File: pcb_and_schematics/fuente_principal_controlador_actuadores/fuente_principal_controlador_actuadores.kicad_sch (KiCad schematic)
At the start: 79 parts, among them J1 Screw_Terminal_01x02, J1 USB3_A 1, J10 Screw_Terminal_01x02, J2 Screw_Terminal_01x02, J2 USB3_A 2, J3 Screw_Terminal_01x02, J3 USB3_A 3, J4 Screw_Terminal_01x02, J4 USB3_A 4, J5 Screw_Terminal_01x02, J6 Screw_Terminal_01x02, J7 Screw_Terminal_01x02, J8 Screw_Terminal_01x02, J9 Screw_Terminal_01x02, Q1 TIP122, Q2 TIP122, Q3 TIP122, Q4 TIP122, Q5 TIP122, Q6 TIP122, Q7 TIP122, Q8 TIP122, U1 40106, U1 LM7812_TO220, U11 40106, U2 LM7805_TO220, U22 40106, U3 LM1117-3.3, U33 40106, U44 40106, U55 40106, U66 40106

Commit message: new footprints added to the schematics, and save process before reestructuration of trigger schmith footprint and schematic
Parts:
- removed J1: USB3_A 1, symbol Connector:USB3_A
- removed J2: USB3_A 2, symbol Connector:USB3_A
- removed J3: USB3_A 3, symbol Connector:USB3_A
- removed J4: USB3_A 4, symbol Connector:USB3_A
- added J1, J2, J3, J4: USB_A, Connector_USB:USB_A_Molex_67643_Horizontal, symbol Connector:USB_A
- J11, J12: renamed from J?; footprint (none) -> Connector_PinSocket_1.27mm:PinSocket_1x15_P1.27mm_Vertical
- R_actuator1, R_actuator2, R_actuator3, R_actuator4, R_actuator5, R_actuator6, R_actuator7, R_actuator9, Rsensor1, Rsensor2: footprint (none) -> Resistor_THT:R_Axial_DIN0204_L3.6mm_D1.6mm_P5.08mm_Horizontal
- Rpullup1, Rpullup2, Rpullup3, Rpullup4, Rpullup5, Rpullup6, Rpullup7, Rpullup8, Rtransistor1, Rtransistor2, Rtransistor3, Rtransistor4, Rtransistor5, Rtransistor6, Rtransistor7, Rtransistor8: footprint (none) -> Resistor_THT:R_Axial_DIN0207_L6.3mm_D2.5mm_P7.62mm_Horizontal
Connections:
- net 3.3VDC: now also J2.1 (VBUS), J3.1 (VBUS), J4.1 (VBUS)
- net GND 3.3V: now also J2.4 (GND), J3.4 (GND), J4.4 (GND)
- net GND ec: now also J1.4 (GND)
- net Signal ExtraSensor: now also J4.3 (D+)
- net signal DB18B20: now also J2.3 (D+)
- net signal EC: now also J1.1 (VBUS), J1.3 (D+)
- net signal PH: now also J3.3 (D+)
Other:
- moved on the sheet: J10, J3, J4, J5, J6, J7, J8, J9, Opto1, Opto2, Opto3, Opto4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

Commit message: everything looks kinda ready for pcb fixies
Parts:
- removed J3, J4: Screw_Terminal_01x02, symbol Connector:Screw_Terminal_01x02
- removed Opto1, Opto2: 4N25, Package_DIP:DIP-6_W7.62mm, symbol Isolator:4N25
- removed Q1, Q2: TIP122, Package_TO_SOT_THT:TO-220-3_Vertical, symbol Transistor_BJT:TIP122
- removed R_actuator1, R_actuator2: 220 ohm, Resistor_THT:R_Axial_DIN0204_L3.6mm_D1.6mm_P5.08mm_Horizontal, symbol Device:R
- removed Rpullup1, Rpullup2: 10k ohm, Resistor_THT:R_Axial_DIN0207_L6.3mm_D2.5mm_P7.62mm_Horizontal, symbol Device:R
- removed Rtransistor1, Rtransistor2: 10 ohm, Resistor_THT:R_Axial_DIN0207_L6.3mm_D2.5mm_P7.62mm_Horizontal, symbol Device:R
- removed U1, U11, U22, U33, U44, U55, U66: 40106, symbol 4xxx:40106
- removed unit 2 of U2
- added J5, J8: Screw_Terminal_01x02, maticas:actuators_screws_01x02_low_pot, symbol Connector:Screw_Terminal_01x02
- added Opto3, Opto6: 4N25, Package_DIP:DIP-6_W7.62mm, symbol Isolator:4N25
- added Q3, Q6: TIP122, Package_TO_SOT_THT:TO-220-3_Vertical, symbol Transistor_BJT:TIP122
- added R_actuator3, R_actuator6: 220 ohm, Resistor_THT:R_Axial_DIN0204_L3.6mm_D1.6mm_P5.08mm_Horizontal, symbol Device:R
- added Rpullup3, Rpullup6: 10k ohm, Resistor_THT:R_Axial_DIN0207_L6.3mm_D2.5mm_P7.62mm_Horizontal, symbol Device:R
- added Rtransistor3, Rtransistor6: 10 ohm, Resistor_THT:R_Axial_DIN0207_L6.3mm_D2.5mm_P7.62mm_Horizontal, symbol Device:R
- added U11, U22: 40106_maticas_full, maticas:40106_maticas_full, symbol maticas:40106_maticas_full
- D3: footprint (none) -> LED_THT:LED_D3.0mm
- J1, J2: footprint (none) -> maticas:actuators_screws_01x02_low_pot
- J10: renamed from J6; footprint (none) -> maticas:actuators_screws_01x02_low_pot
- J3: renamed from J9; footprint (none) -> maticas:actuators_screws_01x02_low_pot
- J4: renamed from J10; footprint (none) -> maticas:actuators_screws_01x02_low_pot
- J6: renamed from J7; footprint (none) -> maticas:actuators_screws_01x02_low_pot
- J7: renamed from J8; footprint (none) -> maticas:actuators_screws_01x02_low_pot
- J9: renamed from J5; footprint (none) -> maticas:actuators_screws_01x02_low_pot
- U3: footprint (none) -> Package_TO_SOT_THT:TO-220-3_Vertical
- renumbered J1 to JUSB1, J2 to JUSB2, J3 to JUSB3, J4 to JUSB5, Opto7 to Opto1, Opto8 to Opto2, Opto5 to Opto4, Opto6 to Opto5, Opto3 to Opto7, Opto4 to Opto8, Q7 to Q1, Q8 to Q2, Q5 to Q4, Q6 to Q5, Q3 to Q7, Q4 to Q8, R_actuator7 to R_actuator1, R_actuator9 to R_actuator2, R_actuator5 to R_actuator4, R_actuator6 to R_actuator5, R_actuator3 to R_actuator7, R_actuator4 to R_actuator8, Rpullup7 to Rpullup1, Rpullup8 to Rpullup2, Rpullup5 to Rpullup4, Rpullup6 to Rpullup5, Rpullup3 to Rpullup7, Rpullup4 to Rpullup8, Rtransistor7 to Rtransistor1, Rtransistor8 to Rtransistor2, Rtransistor5 to Rtransistor4, Rtransistor6 to Rtransistor5, Rtransistor3 to Rtransistor7, Rtransistor4 to Rtransistor8
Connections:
- net 12.0VDC: now also Q6.2 (C), Rpullup6.2, U11.14 (VDD)
- net 3.3V DC esp32: now also Opto3.2
- net 5.0VDC: now also Q3.2 (C), Rpullup3.2, U22.14 (VDD)
- net GND 3.3V: now also Opto6.2
- net GND potencia: now also J5.2 (Pin_2), J8.2 (Pin_2), Opto3.4, Opto6.4, U11.7 (VSS), U22.7 (VSS)
- net extraActuator12V: now also R_actuator6.1
- net extraActuator5V: now also R_actuator3.1
- net at Opto5.5, Rpullup5.1: now also U22.5
- net at Rtransistor5.1: now also U22.6
- net at Opto4.5, Rpullup4.1: now also U22.3
- net at Rtransistor7.1: now also U11.4
- net at Opto8.5, Rpullup8.1: now also U11.5
- net at Opto1.5, Rpullup1.1: now also U22.13
- net at Opto7.5, Rpullup7.1: now also U11.3
- net at Opto2.5, Rpullup2.1: now also U22.9
- net at Rtransistor2.1: now also U22.8
- net at Rtransistor1.1: now also U22.12
- net at Rtransistor8.1: now also U11.6
- net at Rtransistor4.1: now also U22.4
- new net: Opto3.1, R_actuator3.2
- new net: Opto6.5, Rpullup6.1, U11.1
- new net: Opto3.5, Rpullup3.1, U22.1
- new net: Q3.1 (B), Rtransistor3.2
- new net: J5.1 (Pin_1), Q3.3 (E)
- new net: Rtransistor3.1, U22.2
- new net: Opto6.1, R_actuator6.2
- new net: J8.1 (Pin_1), Q6.3 (E)
- new net: Rtransistor6.1, U11.2
- new net: Q6.1 (B), Rtransistor6.2
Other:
- moved on the sheet: J10, J3, J4, J6, J7, J9, Opto1, Opto2, Opto4, Opto5, Opto7, Opto8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

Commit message: addition of net classes, and changes in footprint of resistors
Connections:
- net 12.0VDC renamed 12.0VDC pot
- net 5.0VDC renamed 5.0VDC pot
- net GND potencia renamed GND pot

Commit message: reestructuration of the entire pcb for decreasing the occupied space
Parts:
- Q1, Q2, Q3, Q4, Q5, Q6, Q7, Q8, U1, U2, U3: footprint Package_TO_SOT_THT:TO-220-3_Vertical -> maticas:tip122_more_clearence
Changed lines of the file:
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@@
       (effects (font (size 1 1)))
     )
-    (property "Footprint" "Package_TO_SOT_THT:TO-220-3_Vertical" (id 2) (at 403.225 67.31 0)
+    (property "Footprint" "maticas:tip122_more_clearence" (id 2) (at 403.225 67.31 0)
       (effects (font (size 1.27 1.27) italic) (justify left) hide)
     )
@@
     (property "Reference" "U3" (id 0) (at 113.03 116.84 0))
     (property "Value" "LM1117-3.3" (id 1) (at 113.03 119.38 0))
-    (property "Footprint" "Package_TO_SOT_THT:TO-220-3_Vertical" (id 2) (at 113.03 124.46 0)
+    (property "Footprint" "maticas:tip122_more_clearence" (id 2) (at 113.03 124.46 0)
       (effects (font (size 1.27 1.27)) hide)
     )
@@
       (effects (font (size 1 1)))
     )
-    (property "Footprint" "Package_TO_SOT_THT:TO-220-3_Vertical" (id 2) (at 389.255 152.4 0)
+    (property "Footprint" "maticas:tip122_more_clearence" (id 2) (at 389.255 152.4 0)
       (effects (font (size 1.27 1.27) italic) (justify left) hide)
     )
@@
       (effects (font (size 1 1)))
     )
-    (property "Footprint" "Package_TO_SOT_THT:TO-220-3_Vertical" (id 2) (at 436.245 153.67 0)
+    (property "Footprint" "maticas:tip122_more_clearence" (id 2) (at 436.245 153.67 0)
       (effects (font (size 1.27 1.27) italic) (justify left) hide)
     )
@@
     (property "Reference" "U1" (id 0) (at 114.3 26.67 0))
     (property "Value" "LM7812_TO220" (id 1) (at 114.3 29.21 0))
-    (property "Footprint" "Package_TO_SOT_THT:TO-220-3_Vertical" (id 2) (at 114.3 28.575 0)
+    (property "Footprint" "maticas:tip122_more_clearence" (id 2) (at 114.3 28.575 0)
       (effects (font (size 1.27 1.27) italic) hide)
     )
@@
       (effects (font (size 1 1)))
     )
-    (property "Footprint" "Package_TO_SOT_THT:TO-220-3_Vertical" (id 2) (at 440.055 298.45 0)
+    (property "Footprint" "maticas:tip122_more_clearence" (id 2) (at 440.055 298.45 0)
       (effects (font (size 1.27 1.27) italic) (justify left) hide)
     )
@@
       (effects (font (size 1 1)))
     )
-    (property "Footprint" "Package_TO_SOT_THT:TO-220-3_Vertical" (id 2) (at 497.205 67.31 0)
+    (property "Footprint" "maticas:tip122_more_clearence" (id 2) (at 497.205 67.31 0)
       (effects (font (size 1.27 1.27) italic) (justify left) hide)
     )
@@
       (effects (font (size 1 1)))
     )
-    (property "Footprint" "Package_TO_SOT_THT:TO-220-3_Vertical" (id 2) (at 487.045 300.99 0)
+    (property "Footprint" "maticas:tip122_more_clearence" (id 2) (at 487.045 300.99 0)
       (effects (font (size 1.27 1.27) italic) (justify left) hide)
     )
@@
     (property "Reference" "U2" (id 0) (at 113.03 72.39 0))
     (property "Value" "LM7805_TO220" (id 1) (at 113.03 74.93 0))
-    (property "Footprint" "Package_TO_SOT_THT:TO-220-3_Vertical" (id 2) (at 113.03 74.295 0)
+    (property "Footprint" "maticas:tip122_more_clearence" (id 2) (at 113.03 74.295 0)
       (effects (font (size 1.27 1.27) italic) hide)
     )
@@
       (effects (font (size 1 1)))
     )
-    (property "Footprint" "Package_TO_SOT_THT:TO-220-3_Vertical" (id 2) (at 393.065 299.72 0)
+    (property "Footprint" "maticas:tip122_more_clearence" (id 2) (at 393.065 299.72 0)
       (effects (font (size 1.27 1.27) italic) (justify left) hide)
     )
@@
       (effects (font (size 1 1)))
     )
-    (property "Footprint" "Package_TO_SOT_THT:TO-220-3_Vertical" (id 2) (at 483.235 152.4 0)
+    (property "Footprint" "maticas:tip122_more_clearence" (id 2) (at 483.235 152.4 0)
       (effects (font (size 1.27 1.27) italic) (justify left) hide)
     )
@@
     )
     (path "/0ebe0178-dd09-4168-8aa6-5d2256b17510"
-      (reference "Q1") (unit 1) (value "TIP122") (footprint "Package_TO_SOT_THT:TO-220-3_Vertical")
+      (reference "Q1") (unit 1) (value "TIP122") (footprint "maticas:tip122_more_clearence")
     )
     (path "/babc3b09-80f7-4e5d-8f80-f57767030b56"
-      (reference "Q2") (unit 1) (value "TIP122") (footprint "Package_TO_SOT_THT:TO-220-3_Vertical")
+      (reference "Q2") (unit 1) (value "TIP122") (footprint "maticas:tip122_more_clearence")
     )
     (path "/32f4c8e4-72d2-48d6-855c-61bc63f99a91"
-      (reference "Q3") (unit 1) (value "TIP122") (footprint "Package_TO_SOT_THT:TO-220-3_Vertical")
+      (reference "Q3") (unit 1) (value "TIP122") (footprint "maticas:tip122_more_clearence")
     )
     (path "/3642e484-2b28-4a5c-acb8-52d8a2a171e5"
-      (reference "Q4") (unit 1) (value "TIP122") (footprint "Package_TO_SOT_THT:TO-220-3_Vertical")
+      (reference "Q4") (unit 1) (value "TIP122") (footprint "maticas:tip122_more_clearence")
     )
     (path "/ff8f9121-5161-4056-aa37-1da6a4b61d1b"
-      (reference "Q5") (unit 1) (value "TIP122") (footprint "Package_TO_SOT_THT:TO-220-3_Vertical")
+      (reference "Q5") (unit 1) (value "TIP122") (footprint "maticas:tip122_more_clearence")
     )
     (path "/f959d0aa-e170-45c5-bc4d-4f5636c189ac"
-      (reference "Q6") (unit 1) (value "TIP122") (footprint "Package_TO_SOT_THT:TO-220-3_Vertical")
+      (reference "Q6") (unit 1) (value "TIP122") (footprint "maticas:tip122_more_clearence")
     )
     (path "/3eaa0171-74b7-4800-acbe-50a1cd0d1ece"
-      (reference "Q7") (unit 1) (value "TIP122") (footprint "Package_TO_SOT_THT:TO-220-3_Vertical")
+      (reference "Q7") (unit 1) (value "TIP122") (footprint "maticas:tip122_more_clearence")
     )
     (path "/d4d4949f-32f1-4b16-96a3-74741bff63cd"
-      (reference "Q8") (unit 1) (value "TIP122") (footprint "Package_TO_SOT_THT:TO-220-3_Vertical")
+      (reference "Q8") (unit 1) (value "TIP122") (footprint "maticas:tip122_more_clearence")
     )
     (path "/34053ffa-5aa2-4474-9fd3-792cea01175c"
@@
     )
     (path "/3dfa2d43-7bd4-4a56-9698-017b699c4ed6"
-      (reference "U1") (unit 1) (value "LM7812_TO220") (footprint "Package_TO_SOT_THT:TO-220-3_Vertical")
+      (reference "U1") (unit 1) (value "LM7812_TO220") (footprint "maticas:tip122_more_clearence")
     )
     (path "/d6d5ced2-4b87-4b7f-9b09-0312f18e7084"
-      (reference "U2") (unit 1) (value "LM7805_TO220") (footprint "Package_TO_SOT_THT:TO-220-3_Vertical")
+      (reference "U2") (unit 1) (value "LM7805_TO220") (footprint "maticas:tip122_more_clearence")
     )
     (path "/27170157-b8ad-451f-8de9-d3d2ae62ae96"
-      (reference "U3") (unit 1) (value "LM1117-3.3") (footprint "Package_TO_SOT_THT:TO-220-3_Vertical")
+      (reference "U3") (unit 1) (value "LM1117-3.3") (footprint "maticas:tip122_more_clearence")
     )
     (path "/e4375f9f-bad6-4c53-89aa-c87692cc06e7"

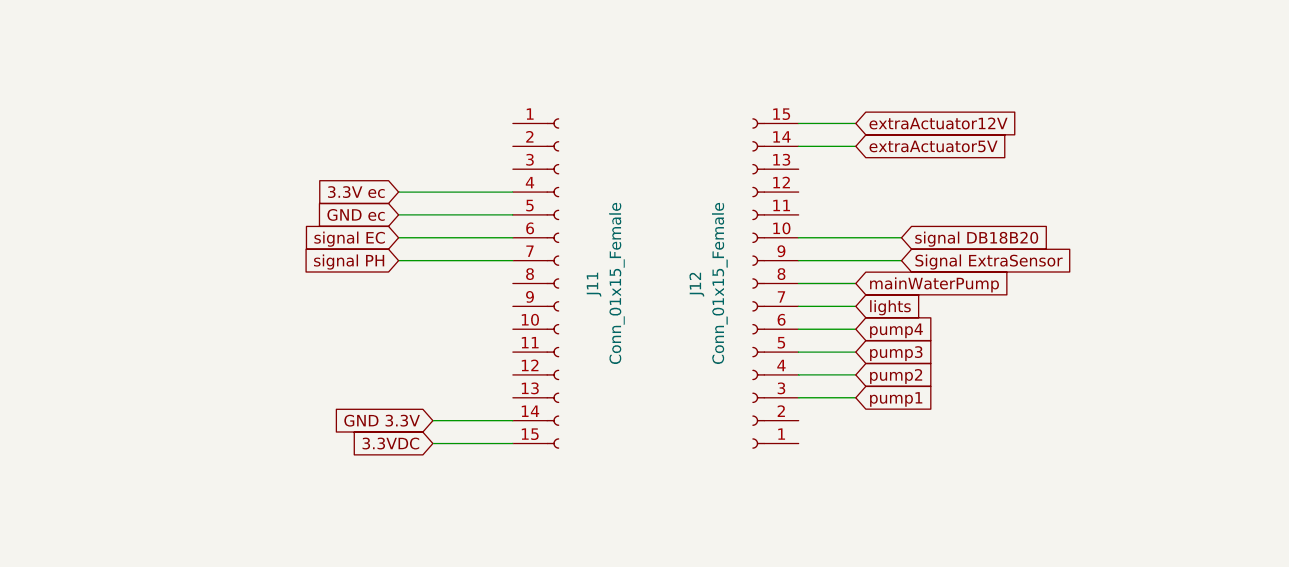
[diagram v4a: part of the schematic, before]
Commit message: reestructuration of pin connections in the schematic
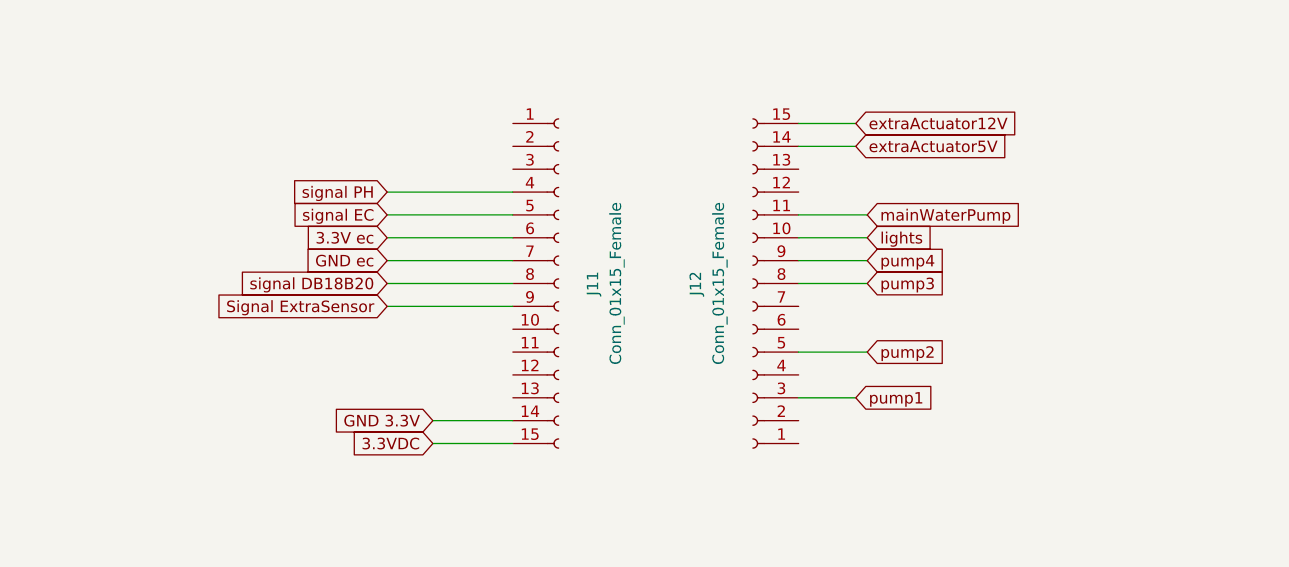
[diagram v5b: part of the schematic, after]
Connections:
- net 3.3V ec: now also J11.6 (Pin_6); no longer J11.4 (Pin_4)
- net GND ec: now also J11.7 (Pin_7); no longer J11.5 (Pin_5)
- net Signal ExtraSensor: now also J11.9 (Pin_9); no longer J12.9 (Pin_9)
- net lights: now also J12.10 (Pin_10); no longer J12.7 (Pin_7)
- net mainWaterPump: now also J12.11 (Pin_11); no longer J12.8 (Pin_8)
- net pump2: now also J12.5 (Pin_5); no longer J12.4 (Pin_4)
- net pump3: now also J12.8 (Pin_8); no longer J12.5 (Pin_5)
- net pump4: now also J12.9 (Pin_9); no longer J12.6 (Pin_6)
- net signal DB18B20: now also J11.8 (Pin_8); no longer J12.10 (Pin_10)
- net signal EC: now also J11.5 (Pin_5); no longer J11.6 (Pin_6)
- net signal PH: now also J11.4 (Pin_4); no longer J11.7 (Pin_7)

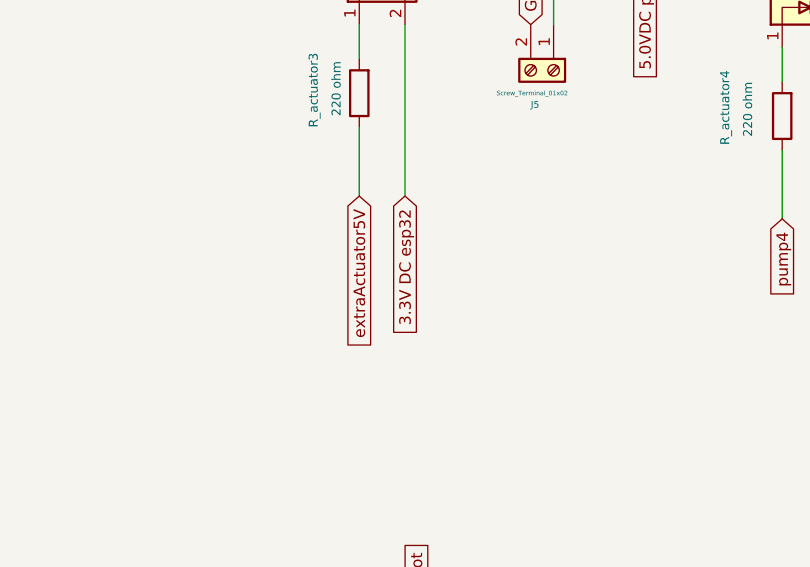
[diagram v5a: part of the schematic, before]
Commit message: reestructuration of pin connections in the schematic, addition of shared ground lines, and recrease in anchor by 1 cm
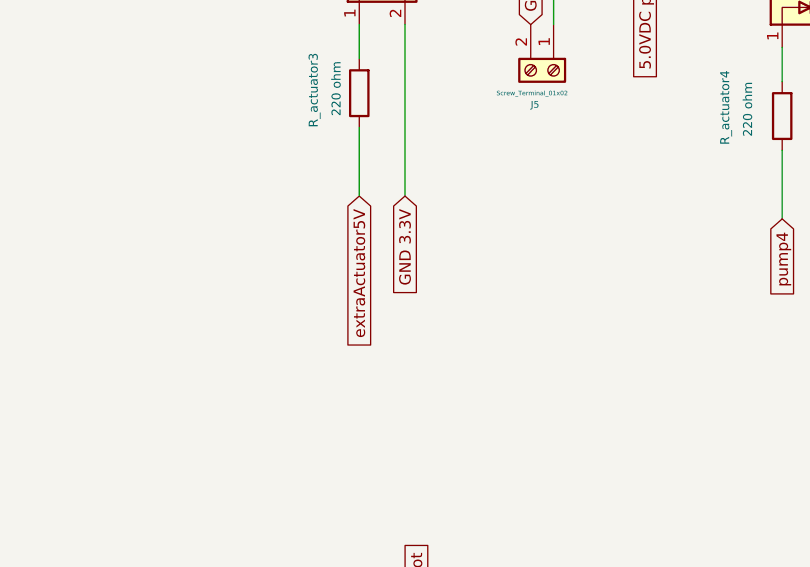
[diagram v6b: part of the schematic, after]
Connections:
- net 3.3V DC esp32 is gone; now on net GND 3.3V: Opto3.2
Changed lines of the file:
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@@
     )
   )
-  (global_label "3.3V DC esp32" (shape input) (at 369.57 186.69 270) (fields_autoplaced)
+  (global_label "GND 3.3V" (shape input) (at 369.57 186.69 270) (fields_autoplaced)
     (effects (font (size 1.27 1.27)) (justify right))
-    (property "Intersheet References" "${INTERSHEET_REFS}" (id 0) (at 369.6494 203.3755 90)
+    (property "Intersheet References" "${INTERSHEET_REFS}" (id 0) (at 369.4906 198.0536 90)
       (effects (font (size 1.27 1.27)) (justify right) hide)
     )
